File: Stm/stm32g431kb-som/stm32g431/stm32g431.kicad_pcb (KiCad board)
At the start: 4 copper layers, 30 x 26.8 mm, 29 parts, among them J1 Conn_ARM_JTAG_SWD_10, J2 USB_C_Receptacle_USB2.0_16P, U1 STM32G431KBTx, U2 AP7361C-33E, Y2 24Mhz

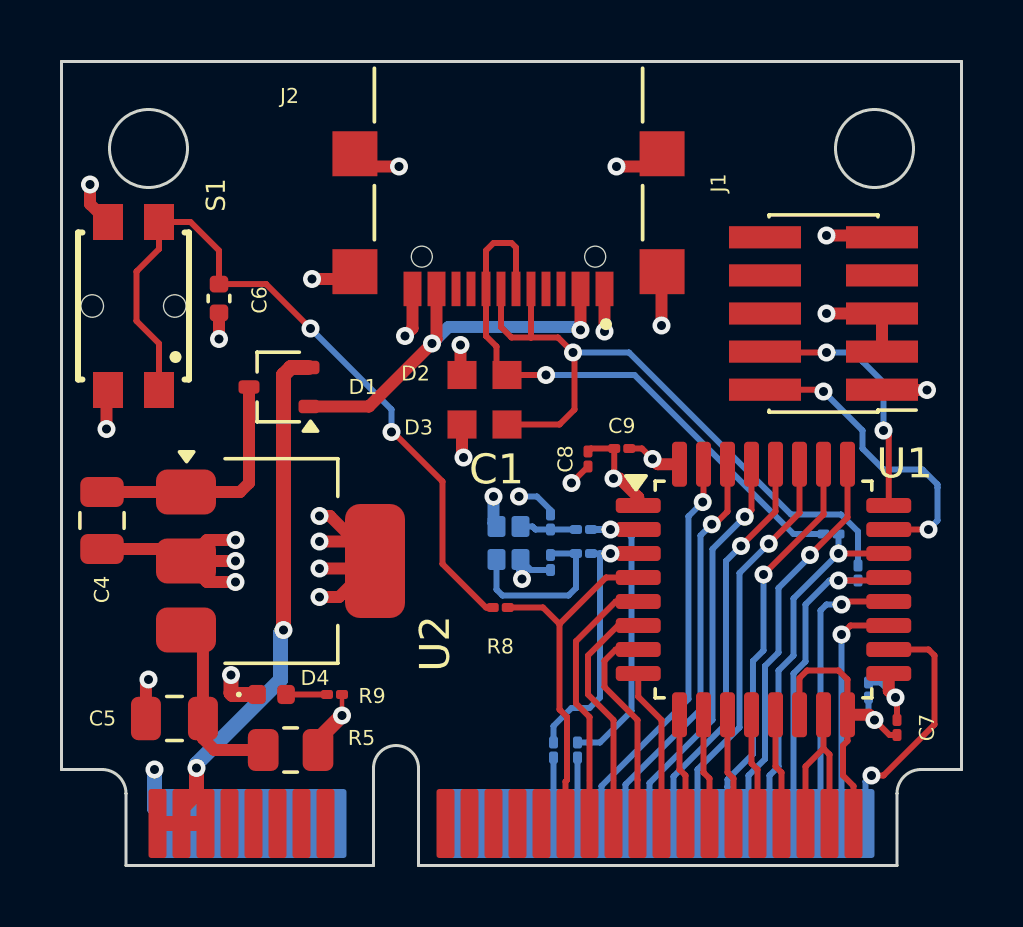
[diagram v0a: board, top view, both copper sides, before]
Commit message: Board layout
Corrected footprints to use 0402
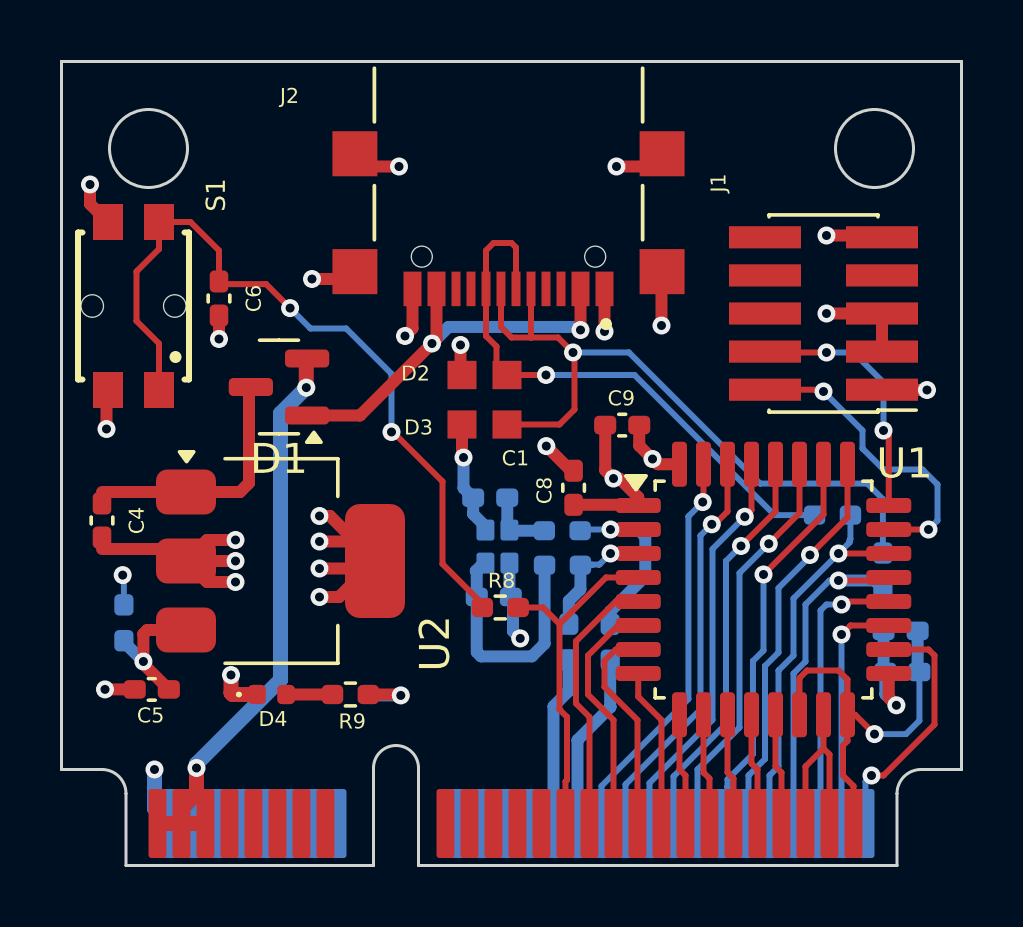
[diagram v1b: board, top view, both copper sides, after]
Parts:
- C10, C8, C9: footprint Capacitor_SMD:C_01005_0402Metric -> Capacitor_SMD:C_0402_1005Metric_Pad0.74x0.62mm_HandSolder
- C2, C3: value C -> 15pF; footprint Capacitor_SMD:C_01005_0402Metric -> Capacitor_SMD:C_0402_1005Metric_Pad0.74x0.62mm_HandSolder
- C4, C5: footprint Capacitor_SMD:C_0805_2012Metric -> Capacitor_SMD:C_0402_1005Metric_Pad0.74x0.62mm_HandSolder
- C6: footprint Capacitor_SMD:C_0402_1005Metric -> Capacitor_SMD:C_0402_1005Metric_Pad0.74x0.62mm_HandSolder
- C7: footprint Capacitor_SMD:C_01005_0402Metric -> Capacitor_SMD:C_0402_1005Metric_Pad0.74x0.62mm_HandSolder; moved to B.Cu
- D1: footprint Package_TO_SOT_SMD:SOT-323_SC-70 -> Package_TO_SOT_SMD:SOT-23
- R1, R2, R3, R4, R6, R7, R8, R9: footprint Resistor_SMD:R_01005_0402Metric -> Resistor_SMD:R_0402_1005Metric_Pad0.72x0.64mm_HandSolder
- R5: footprint Resistor_SMD:R_0805_2012Metric -> Resistor_SMD:R_0402_1005Metric_Pad0.72x0.64mm_HandSolder; moved to B.Cu
- moved R5 6.99 mm to (139.6, 92.3), turned to 90 degrees
- moved R2 3.75 mm to (155.8, 93.0)
- moved R4 3.64 mm to (154.4, 93.0)
- moved C10 2.24 mm to (165.5, 92.6), turned to 0 degrees
- moved C3 2.21 mm to (151.9, 91.5), turned to 0 degrees
- moved C2 2.17 mm to (151.8, 88.1), turned to 180 degrees
- moved C7 1.86 mm to (165.5, 94.0), turned to 0 degrees
- moved C5 1.23 mm to (140.5, 94.5)
- moved C8 1.07 mm to (154.6, 87.8), turned to 90 degrees
- moved R6 0.83 mm to (164.9, 90.6)
- moved R3 0.80 mm to (154.2, 90.4)
- moved C9 0.78 mm to (156.2, 85.7)
- moved R1 0.71 mm to (154.2, 89.2)
- moved R7 0.63 mm to (163.2, 88.7)
- moved R9 0.53 mm to (147.1, 94.7)
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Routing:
- net /PF1: track 8.87 -> 4.21 mm
- net GND: track 61.3 -> 65.8 mm, vias 29 -> 27
- net /PF0: track 11.1 -> 6.62 mm
- net +3V3: track 9.74 -> 13.6 mm, vias 4 -> 5
- net /PFR0: track 2.20 -> 5.90 mm
- net /PFR1: track 2.20 -> 5.66 mm
- net /OSC_OUT: track 5.86 -> 8.26 mm
- net Net-(U2-VO): track 6.07 -> 4.64 mm, vias 0 -> 1
- net /DM: track 22.3 -> 23.3 mm
- net /PA11: track 11.3 -> 12.2 mm
- net /DP: track 21.2 -> 20.7 mm

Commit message: routing
Update board routing
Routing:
- net +3V3: track 13.6 -> 12.8 mm
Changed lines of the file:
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@@
 		(tags "SOT TO_SOT_SMD")
 		(property "Reference" "D1"
-			(at 0 -2.4 180)
+			(at -2.53 0.42 180)
 			(layer "F.SilkS")
 			(effects
 				(font
-					(size 1 1)
-					(thickness 0.15)
+					(size 0.5 0.5)
+					(thickness 0.0625)
 				)
 			)
@@
 		)
 		(embedded_fonts no)
-		(model "${KICAD_USER_3D_MODELS}/PGB1010603NR.step"
+		(model "${KICAD_USER_3D_MODELS_DIR}/PGB1010603NR.step"
 			(offset
 				(xyz 0 0 0)
@@
 		)
 		(embedded_fonts no)
-		(model "${KICAD_USER_3D_MODELS}/PGB1010603NR.step"
+		(model "${KICAD_USER_3D_MODELS_DIR}/PGB1010603NR.step"
 			(offset
 				(xyz 0 0 0)
@@
 	)
 	(segment
-		(start 145.6875 83.5)
-		(end 145.6875 83.813046)
-		(width 0.2)
-		(layer "F.Cu")
-		(net 3)
-	)
-	(segment
 		(start 145.66 83.5275)
 		(end 145.6875 83.5)
@@
 	)
 	(segment
-		(start 144.8 92.65)
+		(start 144.8 94.048)
 		(end 144.8 85.33)
 		(width 0.5)
@@
 	)
 	(segment
-		(start 144.8 94.048)
-		(end 144.8 92.65)
-		(width 0.5)
-		(layer "B.Cu")
-		(net 3)
-	)
-	(segment
 		(start 156.7575 86.4075)
 		(end 157.2 86.85)
@@
 	)
 	(segment
-		(start 147.93 94.73)
-		(end 148.81 94.73)
-		(width 0.4)
-		(layer "B.Cu")
-		(net 35)
-	)
-	(segment
 		(start 139.58 90.76)
 		(end 139.54 90.72)
@@
 	)
 	(segment
-		(start 151.3425 90.6125)
-		(end 151.3425 91.45)
-		(width 0.4)
-		(layer "B.Cu")
-		(net 42)
-	)
-	(segment
 		(start 153.18 93.43)
 		(end 151.485 93.43)
@@
 	)
 	(segment
-		(start 151.57 90.32)
-		(end 151.31 90.58)
-		(width 0.4)
-		(layer "B.Cu")
-		(net 42)
-	)
-	(segment
-		(start 151.31 90.58)
-		(end 151.3425 90.6125)
+		(start 151.3425 90.6075)
+		(end 151.63 90.32)
 		(width 0.4)
 		(layer "B.Cu")
@@
 		(width 0.4)
 		(layer "B.Cu")
+		(net 42)
+	)
+	(segment
+		(start 151.3425 91.45)
+		(end 151.3425 90.6075)
+		(width 0.4)
+		(layer "B.Cu")

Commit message: dirctories
Add and remove directories
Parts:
- D1: value BAT54CW -> BAT54C
- moved S1 0.22 mm to (139.7, 81.8)
- moved D1 0.05 mm to (144.7, 84.4)
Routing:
- net Net-(U2-VI): track 8.22 -> 7.17 mm
